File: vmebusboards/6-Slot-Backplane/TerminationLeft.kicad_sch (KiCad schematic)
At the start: 25 parts, among them U3 OPAMP_8-pin_Generic

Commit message: Updated
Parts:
- added C15: 0.1uF, symbol Device:C_Small
- added C16: 4.7uF, Capacitor_THT:CP_Radial_D5.0mm_P2.00mm, symbol Device:C_Polarized_Small_US
- added JP3, JP4: PASSIVE/ACTIVE, Connector_PinHeader_2.54mm:PinHeader_1x02_P2.54mm_Vertical, symbol Jumper:Jumper_3_Bridged12
- added R19: 330, symbol Device:R_Small
- added R20: 470, symbol Device:R_Small
- added unit 2 of U1
- C14: footprint (none) -> Capacitor_THT:CP_Radial_D5.0mm_P2.00mm
- JP1, JP2: footprint (none) -> Connector_PinHeader_2.54mm:PinHeader_1x02_P2.54mm_Vertical
- RN1, RN10, RN11, RN12, RN2, RN3, RN4, RN5, RN6, RN7, RN8, RN9: symbol Computie_Transceivers:R_Network_Dividers_x08_SIP_Small -> Computie_Miscellaneous:R_Network_Dividers_x08_SIP_Small
- renumbered U3 to U1
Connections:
- net +5V: now also C15.1, JP3.1 (A), R19.1
- net GND: now also C15.2, C16.2, JP4.1 (A), R20.2
- net TERM0_HIGH renamed TERM_L1_HIGH
- net TERM_L1_HIGH: now also RN10.10 (COM2), RN11.10 (COM2), RN12.10 (COM2), RN5.10 (COM2), RN9.10 (COM2)
- net TERM0_LOW renamed TERM_L1_LOW
- net TERM_L1_LOW: now also RN10.1 (COM1), RN11.1 (COM1), RN12.1 (COM1), RN5.1 (COM1), RN9.1 (COM1)
- net TERM1_HIGH renamed TERM_L2_HIGH
- net TERM_L2_HIGH: now also R2.2, JP3.2 (C); no longer RN5.10 (COM2)
- net TERM1_LOW renamed TERM_L2_LOW
- net TERM_L2_LOW: now also R1.1, JP4.2 (C); no longer RN5.1 (COM1)
- removed net TERM2_HIGH: R2.2, RN10.10 (COM2), RN11.10 (COM2), RN12.10 (COM2), RN9.10 (COM2)
- removed net TERM2_LOW: R1.1, RN10.1 (COM1), RN11.1 (COM1), RN12.1 (COM1), RN9.1 (COM1)
- new net: R19.2, R20.1, U1.6 (-)
- new net: C16.1, JP3.3 (B), JP4.3 (B), U1.5 (+), U1.7
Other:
- note removed: "NOTE: the standard says SERCLK and SERDATA are not required to have resistor networks, but the backplane I have pulls them up to 3V so not sure what to do for them"

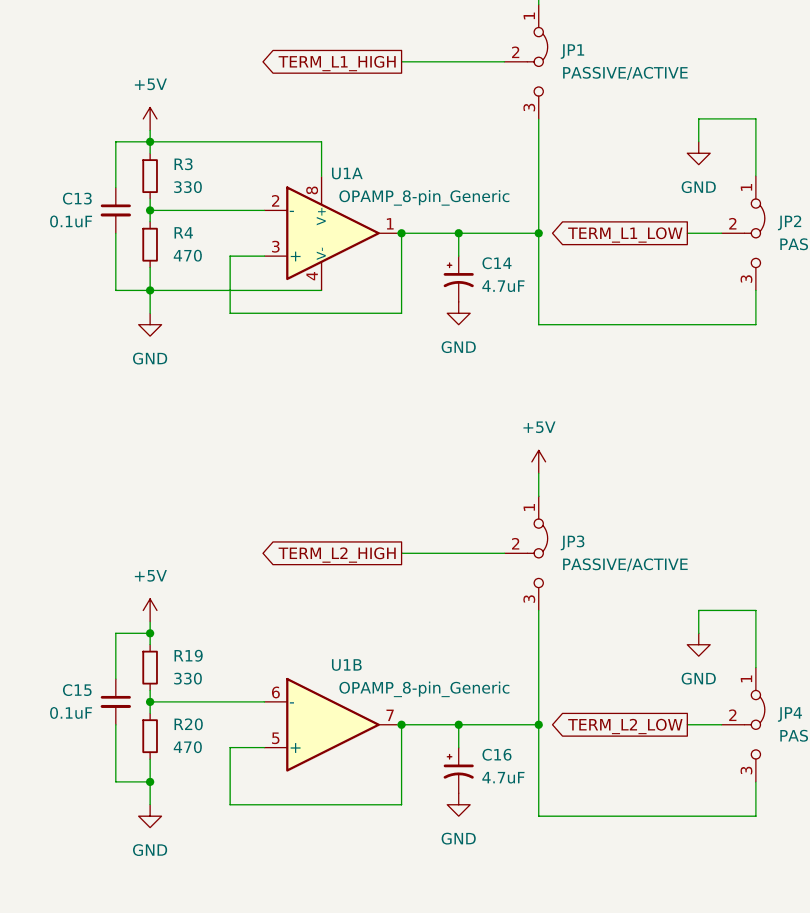
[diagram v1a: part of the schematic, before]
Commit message: Added SystemBoardSMT, renamed k30 boards, and added progress
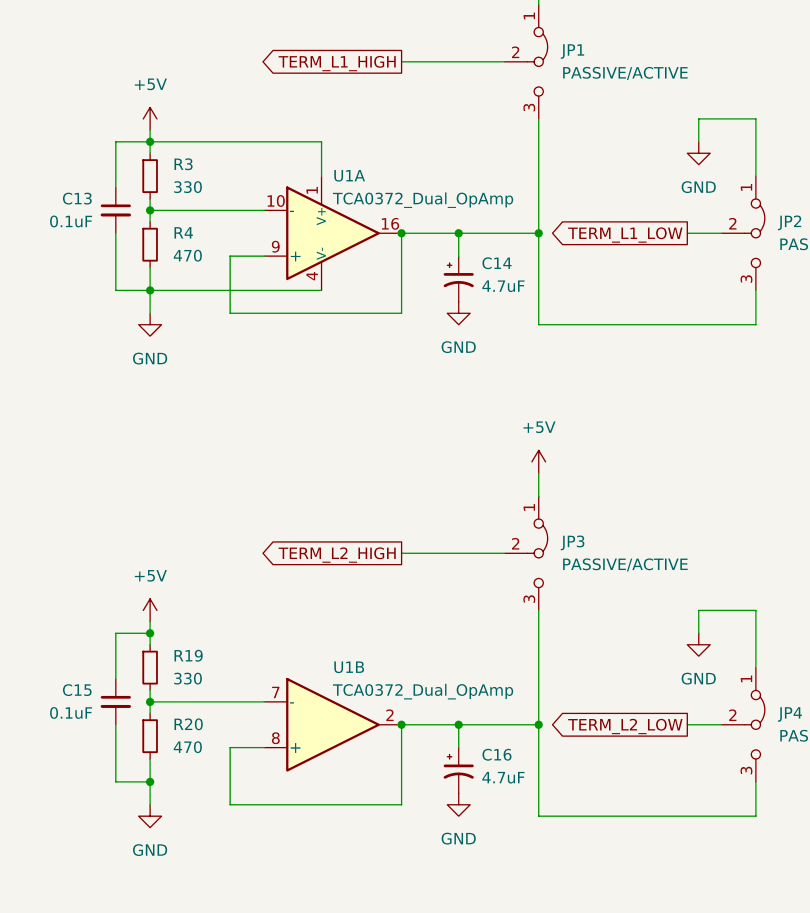
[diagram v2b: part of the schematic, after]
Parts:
- R1, R19, R2, R20, R3, R4: footprint (none) -> Resistor_SMD:R_0805_2012Metric_Pad1.20x1.40mm_HandSolder
- RN1, RN10, RN11, RN12, RN2, RN3, RN4, RN5, RN6, RN7, RN8, RN9: footprint Resistor_THT:R_Array_SIP10 -> Connector_PinHeader_2.54mm:PinHeader_1x10_P2.54mm_Vertical
- U1: value OPAMP_8-pin_Generic -> TCA0372_Dual_OpAmp; footprint (none) -> Package_SO:SOIC-16W_7.5x10.3mm_P1.27mm; symbol PCM_Amplifier_Operational_AKL:OPAMP_Dual_Generic -> Computie_Miscellaneous:TCA0372_Dual_OpAmp
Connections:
- net +5V: now also U1.1 (V+); no longer U1.8 (V+)
- net GND: now also U1.12 (V-), U1.13 (V-), U1.5 (V-)
- net at C14.1, JP1.3 (B), JP2.3 (B): now also U1.16, U1.9 (+); no longer U1.1, U1.3 (+)
- net at R19.2, R20.1: now also U1.7 (-); no longer U1.6 (-)
- net at R3.2, R4.1: now also U1.10 (-); no longer U1.2 (-)
- net at C16.1, JP3.3 (B), JP4.3 (B): now also U1.2, U1.8 (+); no longer U1.5 (+), U1.7
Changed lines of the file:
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@@
 			)
 		)
-		(property "Footprint" "Resistor_THT:R_Array_SIP10"
+		(property "Footprint" "Connector_PinHeader_2.54mm:PinHeader_1x10_P2.54mm_Vertical"
 			(at 41.91 86.995 90)
 			(effects
@@
 			)
 		)
-		(property "Footprint" "Resistor_THT:R_Array_SIP10"
+		(property "Footprint" "Connector_PinHeader_2.54mm:PinHeader_1x10_P2.54mm_Vertical"
 			(at 99.06 86.995 90)
 			(effects
@@
 			)
 		)
-		(property "Footprint" ""
+		(property "Footprint" "Resistor_SMD:R_0805_2012Metric_Pad1.20x1.40mm_HandSolder"
 			(at 198.12 107.95 0)
 			(effects
@@
 			)
 		)
-		(property "Footprint" ""
+		(property "Footprint" "Resistor_SMD:R_0805_2012Metric_Pad1.20x1.40mm_HandSolder"
 			(at 198.12 115.57 0)
 			(effects
@@
 			)
 		)
-		(property "Footprint" "Resistor_THT:R_Array_SIP10"
+		(property "Footprint" "Connector_PinHeader_2.54mm:PinHeader_1x10_P2.54mm_Vertical"
 			(at 156.21 86.995 90)
 			(effects
@@
 			)
 		)
-		(property "Footprint" ""
+		(property "Footprint" "Resistor_SMD:R_0805_2012Metric_Pad1.20x1.40mm_HandSolder"
 			(at 198.12 60.96 0)
 			(effects
@@
 			)
 		)
-		(property "Footprint" ""
+		(property "Footprint" "Resistor_SMD:R_0805_2012Metric_Pad1.20x1.40mm_HandSolder"
 			(at 198.12 53.34 0)
 			(effects
@@
 			)
 		)
-		(property "Footprint" "Resistor_THT:R_Array_SIP10"
+		(property "Footprint" "Connector_PinHeader_2.54mm:PinHeader_1x10_P2.54mm_Vertical"
 			(at 99.06 150.495 90)
 			(effects
@@
 	)
 	(symbol
-		(lib_id "PCM_Amplifier_Operational_AKL:OPAMP_Dual_Generic")
+		(lib_id "Computie_Miscellaneous:TCA0372_Dual_OpAmp")
 		(at 217.17 114.3 0)
 		(unit 2)
@@
 		(dnp no)
 		(property "Reference" "U1"
-			(at 219.964 107.696 0)
+			(at 218.44 107.95 0)
 			(effects
 				(font
 					(size 1.27 1.27)
 				)
+				(justify left)
 			)
 		)
-		(property "Value" "OPAMP_8-pin_Generic"
-			(at 228.6 110.236 0)
+		(property "Value" "TCA0372_Dual_OpAmp"
+			(at 218.44 110.49 0)
 			(effects
 				(font
 					(size 1.27 1.27)
 				)
+				(justify left)
 			)
 		)
-		(property "Footprint" ""
+		(property "Footprint" "Package_SO:SOIC-16W_7.5x10.3mm_P1.27mm"
 			(at 217.17 114.3 0)
 			(effects
@@
 		(pin "2"
 		)
-		(pin "3"
+		(pin "9"
 		)
 		(pin "8"
 		)
-		(pin "6"
+		(pin "10"
 		)
 		(pin "4"
@@
 		(pin "1"
 		)
+		(pin "12"
+		)
+		(pin "13"
+		)
+		(pin "16"
+		)
 		(instances
 			(project "6-Slot-Backplane"
@@
 			)
 		)
-		(property "Footprint" "Resistor_THT:R_Array_SIP10"
+		(property "Footprint" "Connector_PinHeader_2.54mm:PinHeader_1x10_P2.54mm_Vertical"
 			(at 41.91 55.245 90)
 			(effects
@@
 			)
 		)
-		(property "Footprint" "Resistor_THT:R_Array_SIP10"
+		(property "Footprint" "Connector_PinHeader_2.54mm:PinHeader_1x10_P2.54mm_Vertical"
 			(at 41.91 150.495 90)
 			(effects
@@
 			)
 		)
-		(property "Footprint" "Resistor_THT:R_Array_SIP10"
+		(property "Footprint" "Connector_PinHeader_2.54mm:PinHeader_1x10_P2.54mm_Vertical"
 			(at 99.06 118.745 90)
 			(effects
@@
 			)
 		)
-		(property "Footprint" "Resistor_THT:R_Array_SIP10"
+		(property "Footprint" "Connector_PinHeader_2.54mm:PinHeader_1x10_P2.54mm_Vertical"
 			(at 41.91 118.745 90)
 			(effects
@@
 			)
 		)
-		(property "Footprint" "Resistor_THT:R_Array_SIP10"
+		(property "Footprint" "Connector_PinHeader_2.54mm:PinHeader_1x10_P2.54mm_Vertical"
 			(at 156.21 55.245 90)
 			(effects
@@
 			)
 		)
-		(property "Footprint" ""
+		(property "Footprint" "Resistor_SMD:R_0805_2012Metric_Pad1.20x1.40mm_HandSolder"
 			(at 154.94 160.02 0)
 			(effects
@@
 			)
 		)
-		(property "Footprint" "Resistor_THT:R_Array_SIP10"
+		(property "Footprint" "Connector_PinHeader_2.54mm:PinHeader_1x10_P2.54mm_Vertical"
 			(at 156.21 118.745 90)
 			(effects
@@
 			)
 		)
-		(property "Footprint" "Resistor_THT:R_Array_SIP10"
+		(property "Footprint" "Connector_PinHeader_2.54mm:PinHeader_1x10_P2.54mm_Vertical"
 			(at 99.06 55.245 90)
 			(effects
@@
 			)
 		)
-		(property "Footprint" ""
+		(property "Footprint" "Resistor_SMD:R_0805_2012Metric_Pad1.20x1.40mm_HandSolder"
 			(at 160.02 162.56 0)
 			(effects
@@
 			)
 		)
-		(property "Footprint" "Resistor_THT:R_Array_SIP10"
+		(property "Footprint" "Connector_PinHeader_2.54mm:PinHeader_1x10_P2.54mm_Vertical"
 			(at 156.21 150.495 90)
 			(effects
@@
 	)
 	(symbol
-		(lib_id "PCM_Amplifier_Operational_AKL:OPAMP_Dual_Generic")
+		(lib_id "Computie_Miscellaneous:TCA0372_Dual_OpAmp")
 		(at 217.17 59.69 0)
 		(unit 1)
@@
 		(dnp no)
 		(property "Reference" "U1"
-			(at 219.964 53.086 0)
+			(at 218.44 53.34 0)
 			(effects
 				(font
 					(size 1.27 1.27)
 				)
+				(justify left)
 			)
 		)
-		(property "Value" "OPAMP_8-pin_Generic"
-			(at 228.6 55.626 0)
+		(property "Value" "TCA0372_Dual_OpAmp"
+			(at 218.44 55.88 0)
 			(effects
 				(font
 					(size 1.27 1.27)
 				)
+				(justify left)
 			)
 		)
-		(property "Footprint" ""
+		(property "Footprint" "Package_SO:SOIC-16W_7.5x10.3mm_P1.27mm"
 			(at 217.17 59.69 0)
 			(effects
@@
 		(pin "2"
 		)
-		(pin "3"
+		(pin "13"
 		)
 		(pin "8"
 		)
-		(pin "6"
+		(pin "16"
 		)
 		(pin "4"
@@
 		(pin "1"
 		)
+		(pin "9"
+		)
+		(pin "10"
+		)
+		(pin "12"
+		)
 		(instances
